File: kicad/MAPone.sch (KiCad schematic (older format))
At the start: 37 parts, among them J1 BARREL_JACK, J2 USB-Micro, P1 CONN_1, P2 CONN_1, P3 CONN_1, P4 CONN_1, SW1 RST, U1 7805, U2 ATMEGA328-P, X1 16MHz

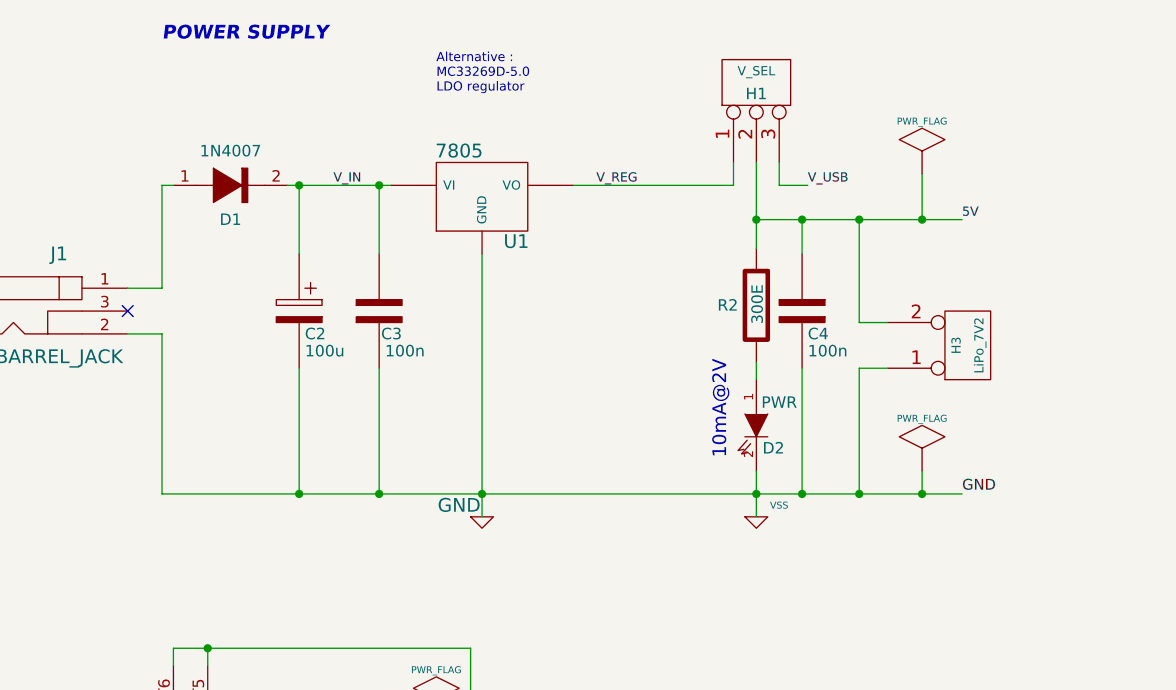
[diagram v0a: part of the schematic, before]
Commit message: MAPone & MAPusart made a common gerbe
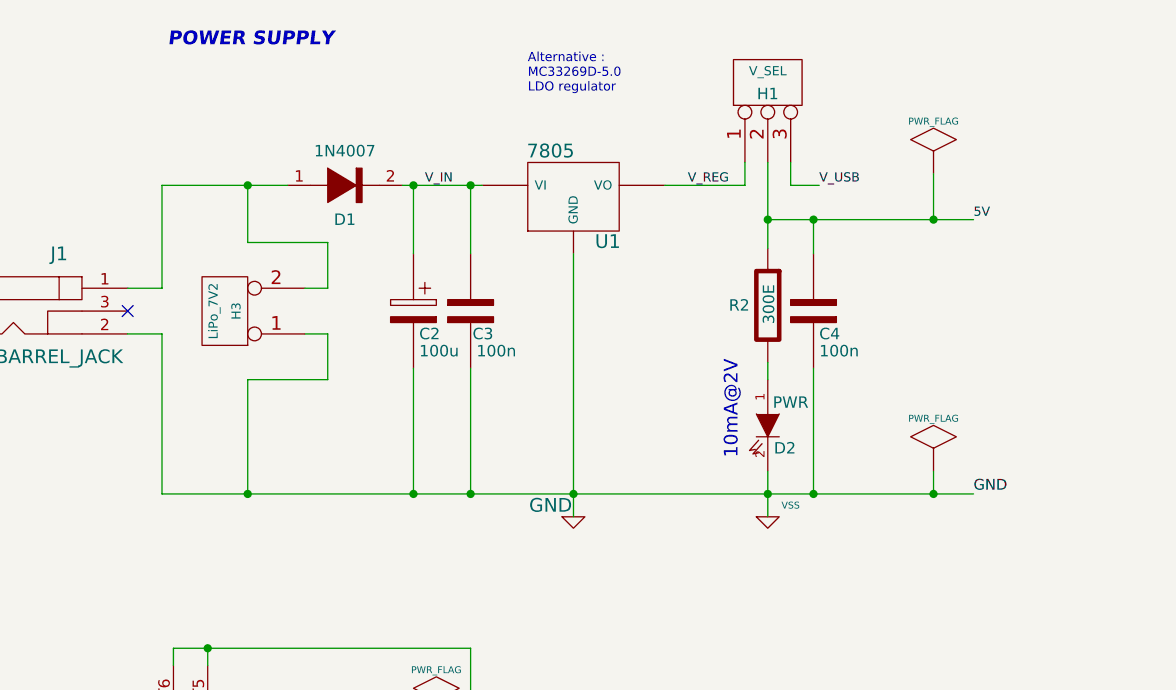
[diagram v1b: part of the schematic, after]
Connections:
- net 5V: no longer H3.2 (PM)
- net at D1.1 (Anode), J1.1: now also H3.2 (PM)
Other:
- moved on the sheet: C2, C3, C4, D1, D2, H1, H3, R2, U1
